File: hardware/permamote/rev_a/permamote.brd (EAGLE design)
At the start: 27 x 60.1 mm, 102 parts, among them J1 TC2030-JLINK-NL, J5 MICRO_USB_B_HIROSE_ZX62R-B-5P, Q1 PMDXB950UPEL, Q10 PMDXB950UPEL, Q2 PMDXB950UPEL, Q3 PMDXB950UPEL, Q4 PMDXB950UPEL, Q5 PMDXB950UPEL, Q6 PMDXB950UPEL, Q7 PMDXB950UPEL, Q8 PMDXB950UPEL, U1 AB1815-T3, U10 NRF52840, U11 SI7021-A20-GM1, U12 FT232RQ, U2 BQ25505, U3 EKMB1101111, U4 ISL29125, U5 LIS2DW12, U6 MAX17222, U7 MAX44009, U8 MS5637-02BA03, X1 32MHz, X3 32.768kHz, X4 ABS07-32.768KHZ-7-T

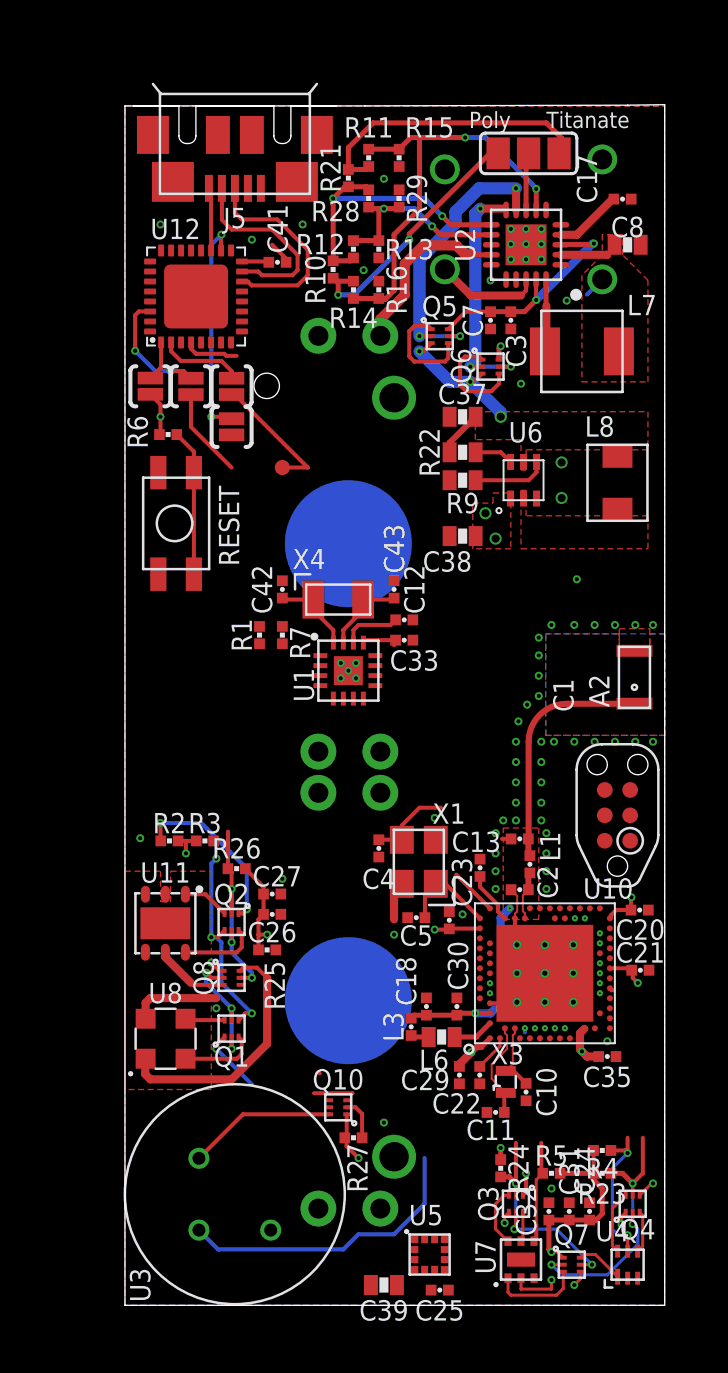
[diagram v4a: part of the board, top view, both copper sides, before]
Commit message: Rearrange board to move light sensors to bottom edge
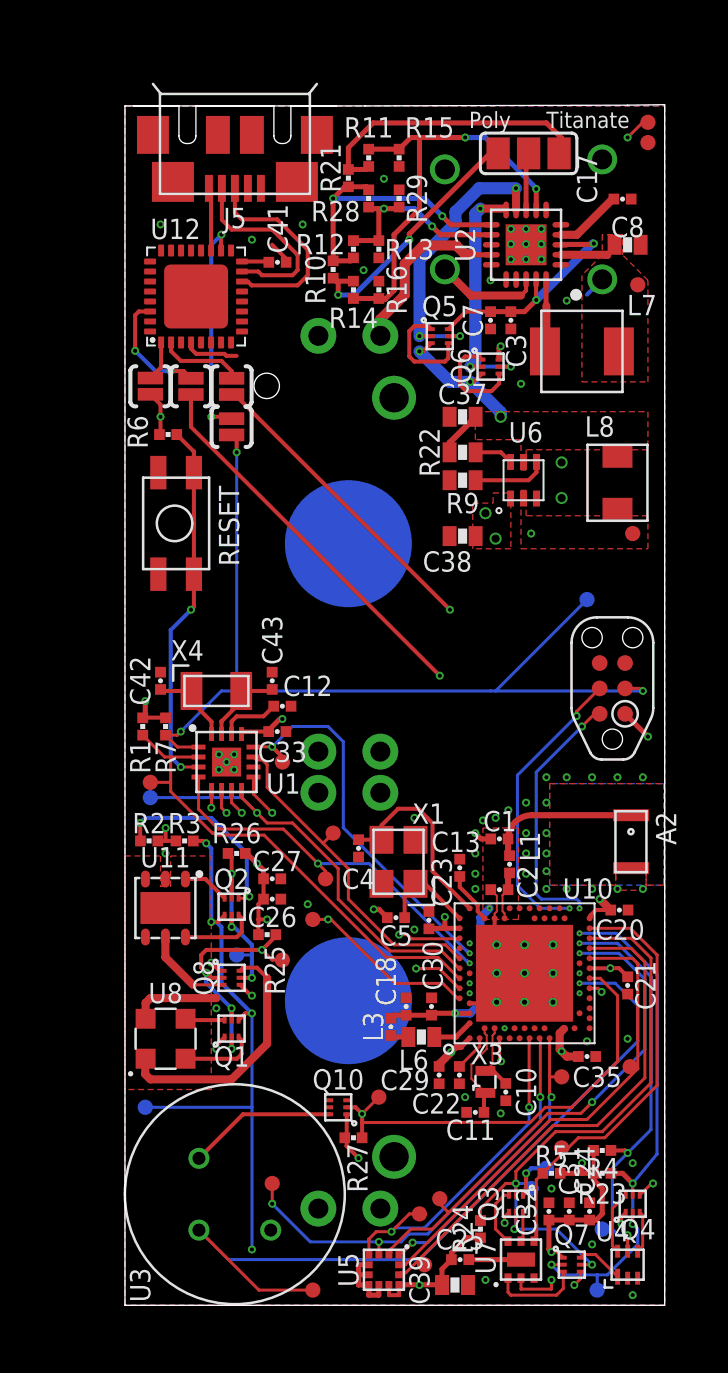
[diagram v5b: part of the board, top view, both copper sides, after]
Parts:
- added TP10, TP11, TP12, TP13, TP14, TP15, TP16, TP17, TP18, TP19, TP2, TP20, TP21, TP22, TP23, TP24, TP25, TP26, TP27, TP3, TP4, TP5, TP6, TP7, TP8, TP9: TEST-POINT3, headers:PAD.03X.03
- moved TP1 32.7 mm to (1.02, 9.91), flipped to the bottom
- moved A2 8.23 mm to (25.3, 23.2), turned to 270 degrees
- moved C33 7.82 mm to (7.62, 28.7)
- moved C42 7.62 mm to (1.78, 31.2)
- moved C43 7.62 mm to (7.37, 31.2)
- moved U1 7.62 mm to (5.08, 27.2)
- moved X4 7.62 mm to (4.57, 30.7)
- moved C12 7.47 mm to (7.87, 30.0)
- moved R1 7.42 mm to (0.89, 29.0)
- moved R7 7.42 mm to (2.03, 29.0)
- moved J1 6.36 mm to (24.4, 30.9)
- moved C39 3.56 mm to (16.5, 1.02), turned to 0 degrees
- moved R24 3.21 mm to (17.8, 3.81), turned to 270 degrees
- moved U5 2.41 mm to (13.0, 1.78), turned to 270 degrees
- moved C25 1.83 mm to (16.8, 2.29)
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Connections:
- net !CLR_EN: now also TP9.P$1
- net !CLR_INT: now also TP20.P$1
- net !HUM_EN: now also TP12.P$1, U10.A20; no longer U10.P2
- net !LT_EN: now also TP10.P$1, U10.AD20; no longer U10.AD16
- net !LT_INT: now also TP21.P$1, U10.AD22; no longer U10.AD18
- net !PIR_EN: now also TP11.P$1, U10.AD12; no longer U10.Y23
- net !PR_EN: now also TP8.P$1, U10.B19; no longer U10.T2
- net !RST: now also TP17.P$1
- net !RTC_IRQ1: now also TP13.P$1, U10.A16; no longer U10.AC11
- net !RTC_IRQ2: now also TP14.P$1, U10.B15; no longer U10.AC15
- net !RTC_IRQ3: now also TP15.P$1, U10.A14; no longer U10.AD12
- net ACC_CS: now also TP7.P$1, U10.AC17; no longer U10.M2
- net ACC_INT1: now also TP18.P$1, U10.AD16; no longer U10.L1
- net ACC_INT2: now also TP19.P$1, U10.AD18; no longer U10.K2
- net DBG_TX: no longer TP1.P$1
- net GND: now also TP27.P$1
- net MISO: now also TP4.P$1, U10.R1; no longer U10.U1
- net MOSI: now also TP5.P$1
- net PIR_OUT: now also TP22.P$1, U10.AC11; no longer U10.V23
- net RTC_CS: now also TP6.P$1, U10.B17; no longer U10.AC9
- net SCK: now also TP3.P$1, U10.U1; no longer U10.R1
- net SCL: now also TP2.P$1, U10.AC9; no longer U10.AD20
- net SDA: now also TP1.P$1, U10.AD10; no longer U10.AD22
- net SW: now also TP25.P$1
- net VBAT: now also U10.A10
- net VCC: now also TP26.P$1
- net VSEC: now also TP24.P$1, U10.A8; no longer U10.J1
- net VSOL: now also TP23.P$1
- net WDI: now also TP16.P$1, U10.A12; no longer U10.AD10
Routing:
- net !RST: track 0.00 -> 67.6 mm, vias 1 -> 4
- net MOSI: track 0.02 -> 45.5 mm, vias 0 -> 3
- net SCK: track 0.00 -> 45.1 mm, vias 0 -> 3
- net MISO: track 0.00 -> 44.5 mm, vias 0 -> 4
- net SDA: track 27.8 -> 68.2 mm, vias 5 -> 7
- net VSOL: track 3.40 -> 42.5 mm
- net DBG_RX: track 4.49 -> 41.0 mm, vias 0 -> 2
- net DBG_TX: track 6.79 -> 37.5 mm, vias 1 -> 2
- net SCL: track 27.7 -> 55.8 mm, vias 5 -> 6
- net VSEC: track 23.5 -> 50.4 mm
- net ACC_INT2: track 0.00 -> 25.7 mm, vias 1 -> 0
- net ACC_CS: track 0.00 -> 25.4 mm, vias 1 -> 2
- net PIR_OUT: track 14.9 -> 39.2 mm
- net ACC_INT1: track 0.00 -> 24.2 mm
- net SW: track 0.00 -> 24.2 mm, vias 1 -> 2
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
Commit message: Add Debug LED
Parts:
- removed U$1: (no value), logos:UCB_CAL_100MIL
- added D2: SML-LX0404SIUPGUSB, leds:1MM_SQ_4PAD
- added R17, R18, R8: 470, passives:0402_RES
- D1: value SOLARCELL -> SOLARCELLHOLES; device mote:SOLAR_HOLES -> permamote:SOLAR_HOLES
- TP1, TP10, TP11, TP12, TP13, TP14, TP15, TP16, TP17, TP18, TP19, TP2, TP20, TP21, TP22, TP23, TP24, TP25, TP26, TP27, TP3, TP4, TP5, TP6, TP7, TP8, TP9: value TEST-POINT3 -> TEST-POINT
- moved U$2 38.1 mm to (6.86, 39.1)
- moved TP2 27.1 mm to (1.02, 25.1), flipped to the top
- moved TP4 7.41 mm to (1.02, 9.91)
- moved TP20 7.27 mm to (25.4, 10.9)
- moved TP15 5.62 mm to (6.60, 23.6)
- moved TP25 4.06 mm to (21.3, 38.6)
- moved D1 3.39 mm to (25.1, 51.2), flipped to the top, turned to 270 degrees
- moved TP11 3.31 mm to (15.5, 8.64)
- moved TP23 2.05 mm to (23.6, 51.3)
- moved TP18 0.63 mm to (25.3, 12.6)
- moved TP13 0.36 mm to (10.2, 23.9)
- moved TP12 0.25 mm to (5.59, 17.8)
- moved TP3 0.25 mm to (21.6, 11.4)
- moved TP7 0.25 mm to (15.7, 5.59)
- moved TP16 0.25 mm to (1.02, 26.2)
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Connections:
- new net LED_BLUE: R18.2, U10.K2
- new net LED_GREEN: R17.2, U10.L1
- new net LED_RED: R8.2, U10.J1
- new net N$15: D2.2, R8.1
- new net N$17: D2.4, R17.1
- new net N$19: D2.3, R18.1
- net VCC: now also D2.1
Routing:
- net LED_GREEN: track 0.00 -> 13.6 mm, vias 0 -> 2
- net LED_BLUE: track 0.00 -> 11.5 mm, vias 0 -> 2
- net LED_RED: track 0.00 -> 8.55 mm, vias 0 -> 2
- net MISO: track 44.5 -> 53.0 mm
- net VCC: track 50.9 -> 57.6 mm, vias 22 -> 23
- net !RTC_IRQ3: track 21.4 -> 17.8 mm
- net N$17: track 0.00 -> 3.14 mm
- net PIR_OUT: track 39.2 -> 36.9 mm
- net N$15: track 0.00 -> 2.28 mm
- net ACC_CS: track 25.4 -> 23.1 mm
- net N$19: track 0.00 -> 2.11 mm
- net !RST: track 67.6 -> 66.0 mm
- net !PIR_EN: track 22.4 -> 21.1 mm
- net !LT_INT: track 21.9 -> 21.0 mm
- net VSOL: track 42.5 -> 41.8 mm
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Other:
- board text added: "Other"
- board text removed: "Poly"

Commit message: Rename passives
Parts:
- removed C35: 4.7uF, passives:0402_CAP
- removed C37, C38, C39: 10uF, passives:0603_CAP
- removed C41: 0.1uF, passives:0402_CAP
- removed C42, C43: DNP, passives:0402_CAP
- removed L8: 1uH, passives:IHL-1212BZ-11
- removed R28: 6.19M, passives:0402_RES
- removed R29: 6.81M, passives:0402_RES
- removed U12: FT232RQ, ftdichip:QFN32
- added C14, C15, C16, C19: 0.1uF, passives:0402_CAP
- added C28: 4.7uF, passives:0603_CAP
- added C6: 12pF, passives:0402_CAP
- added C9: 10nF, passives:0402_CAP
- added L2: 15nH, passives:0402_CAP
- added R19: 7.32M, passives:0402_RES
- added R20: 8.87M, passives:0402_RES
- added U9: MS5637-02BA03, chips:4-SMD
- C10: value 12pF -> 10nF
- C11: value 12pF -> 47nF
- C12: value 47pF -> 0.1uF
- C13: value 100pF -> 0.1uF
- C17: value 10nF -> 0.1uF
- C18: value 47nF -> 0.1uF
- C21, C22, C23, C24, C25: value 0.1uF -> 1uF
- C26, C27: value 0.1uF -> 4.7uF
- C29, C30, C31: value 1uF -> 10uF; device passives:0402_CAP -> passives:0603_CAP
- C3: value 0.01uF -> 12pF
- C32, C33: value 1uF -> DNP
- C7: value 4.7uF -> 47pF
- C8: value 4.7uF -> 100pF; device passives:0603_CAP -> passives:0402_CAP
- L3: value 15nH -> 1uH; device passives:0402_CAP -> passives:IHL-1212BZ-11
- R1, R2, R3: value 10kΩ -> 470
- R10: value 6.04k -> 10k
- R11: value 3.9M -> 10k
- R12: value 8.87M -> 10k
- R13: value 4.22M -> 80.6k; device passives:0402_RES -> passives:0603-RES
- R14: value 7.32M -> 3.9M
- R15: value 9.09M -> 4.22M
- R17: value 470 -> 6.19M
- R18: value 470 -> 6.81M
- R21: value 6.04k -> 9.09M
- R22: value 33MΩ -> 33M
- R23, R24, R25, R26, R27: value 100MΩ -> 100M
- R4, R5: value 10kΩ -> 6.04k
- R6, R7: value 10kΩ -> 10k
- R8: value 470 -> 10k
- R9: value 80.6kΩ -> 10k; device passives:0603-RES -> passives:0402_RES
- U4: value ISL29125 -> FT232RQ; device chips:ODFN-6-1.5MMX1.6MM -> ftdichip:QFN32
- U5: value LIS2DW12 -> ISL29125; device chips:LGA-12 -> chips:ODFN-6-1.5MMX1.6MM
- U6: value MAX17222 -> LIS2DW12; device chips:UDFN-6-MAXIM -> chips:LGA-12
- U7: value MAX44009 -> MAX17222; device chips:UDFN-6-EXPOSED -> chips:UDFN-6-MAXIM
- U8: value MS5637-02BA03 -> MAX44009; device chips:4-SMD -> chips:UDFN-6-EXPOSED
- moved C17 53.7 mm to (16.8, 2.29)
- moved U4 53.0 mm to (3.56, 50.5)
- moved R4 50.3 mm to (11.2, 56.4), turned to 90 degrees
- moved R5 46.5 mm to (10.4, 51.8), turned to 270 degrees
- moved R18 42.8 mm to (13.7, 55.4)
- moved R17 42.8 mm to (12.2, 55.4), turned to 90 degrees
- moved U6 40.1 mm to (13.0, 1.78), turned to 270 degrees
- moved U7 39.0 mm to (19.9, 41.3)
- moved C10 38.6 mm to (19.3, 49.3), turned to 270 degrees
- moved C20 36.6 mm to (7.63, 52.2)
- moved R9 35.0 mm to (21.3, 6.60)
- moved C29 33.0 mm to (16.9, 44.5), turned to 180 degrees
- moved C32 32.9 mm to (1.78, 31.2)
- moved C8 32.3 mm to (16.7, 21.9), turned to 90 degrees
- moved R11 30.2 mm to (2.03, 29.0), turned to 90 degrees
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- renumbered L6 to L4, L7 to L5
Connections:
- net !CLR_INT: now also R8.1, U5.5; no longer R4.1, U4.5
- net !FTDI_RESET: now also U4.18; no longer U12.18
- net !LT_INT: now also R9.1, U8.4; no longer R5.1, U7.4
- net !RST: now also R11.1; no longer R7.1
- net !RTC_EXTR: now also R10.1; no longer R6.1
- net ACC_CS: now also U6.2; no longer U5.2
- net ACC_INT1: now also U6.12; no longer U5.12
- net ACC_INT2: now also U6.11; no longer U5.11
- net D+: now also U4.14; no longer U12.14
- net D-: now also U4.15; no longer U12.15
- net FTDI_VCCIO: now also U4.1; no longer U12.1
- net GND: now also C10.2, C11.2, C14.2, C15.2, C16.2, C19.2, C28.2, C3.1, C6.1, C9.2, R18.1, R21.1, U4.17, U4.20, U4.24, U4.26, U4.4, U5.3, U6.5, U6.6, U6.7, U6.8, U8.2, U8.3, U8.EP, U9.4; no longer C10.1, C11.1, C3.2, C35.2, C37.2, C38.2, C39.2, C41.2, C42.2, C43.2, R29.1, R9.1, U12.17, U12.20, U12.24, U12.26, U12.4, U4.3, U5.5, U5.6, U5.7, U5.8, U6.3, U7.2, U7.EP, U8.4
- net LED_BLUE: now also R3.2; no longer R18.2
- net LED_GREEN: now also R2.2; no longer R17.2
- net LED_RED: now also R1.2; no longer R8.2
- net MISO: now also U6.3; no longer U5.3
- net MOSI: now also U6.4; no longer U5.4
- net N$1: now also R14.2, R4.2; no longer R11.2, R21.2
- net N$12: now also R13.2, U7.4; no longer R9.2, U6.4
- net N$13: now also C20.1, U4.16; no longer C41.1, U12.16
- net N$14: now also U7.6; no longer U6.6
- net N$15: now also R1.1; no longer R8.1
- net N$16: now also R19.2, R5.2; no longer R10.2, R14.2
- net N$17: now also R2.1; no longer R17.1
- net N$18: now also R19.1, R21.2; no longer R11.1, R15.2
- net N$19: now also R3.1; no longer R18.1
- net N$2: now also C14.1; no longer C22.1
- net N$20: now also U8.1; no longer U7.1
- net N$21: now also U9.1; no longer U8.1
- net N$25: now also C7.1; no longer C12.1
- net N$26: now also C32.1; no longer C42.1
- net N$27: now also C33.1; no longer C43.1
- net N$3: now also C11.1, C22.1, L2.1; no longer C18.1, C30.1, L3.1
- net N$31: now also U5.1; no longer U4.1
- net N$34: now also U9.3; no longer U8.3
- net N$4: now also C8.1; no longer C13.1
- net N$41: now also U9.2; no longer U8.2
- net N$49: now also L2.2; no longer L3.2
- net N$51: now also U8.6; no longer U7.6
- net N$52: now also U8.5; no longer U7.5
- net N$54: now also U5.4; no longer U4.4
- net N$55: now also U5.6; no longer U4.6
- net N$57: now also R15.2, R17.1, R18.2, R20.1; no longer R12.1, R13.2, R28.1, R29.2
- net N$58: now also R17.2, R20.2, R4.1, R5.1; no longer R10.1, R12.2, R21.1, R28.2
- net N$8: now also C3.2; no longer C4.2
- net N$9: now also C4.2; no longer C5.2
- net RXD: now also U4.2; no longer U12.2
- net SCK: now also U6.1; no longer U5.1
- net SCL: now also R6.1; no longer R2.1
- net SDA: now also R7.1; no longer R3.1
- net SW: now also L3.P$2, U7.2; no longer L8.P$2, U6.2
- net TXD: now also U4.30; no longer U12.30
- net USB_5V: now also U4.19; no longer U12.19
- net VCC: now also C12.1, C13.1, C15.1, C16.1, C17.1, C18.1, C19.1, C30.1, R10.2, R11.2, R12.2, R8.2, R9.2, U6.10, U6.9, U7.1; no longer C20.1, C27.1, C29.1, C32.1, C33.1, C35.1, C38.1, C39.1, R1.2, R2.2, R3.2, R4.2, R5.2, U5.10, U5.9, U6.1
- net VOC_SAMP_VSTOR: now also C10.1, C27.1; no longer C3.1, C7.1
- net VREF_SAMP: now also C9.1; no longer C17.1
- net VSOL: now also C28.1; no longer C8.1
- net VSW: now also C29.1, L3.P$1, U7.5; no longer C37.1, L8.P$1, U6.5
- net WDI: now also R12.1; no longer R1.1
- net XL1: now also C6.2; no longer C11.2
- net XL2: now also C5.2; no longer C10.2
